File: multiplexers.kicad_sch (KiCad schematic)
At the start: 12 parts, among them U2 CD74HC4067M, U3 CD74HC4067M, U4 CD74HC4067M, U5 CD74HC4067M, U7 CD74HC4067M, U8 CD74HC4067M

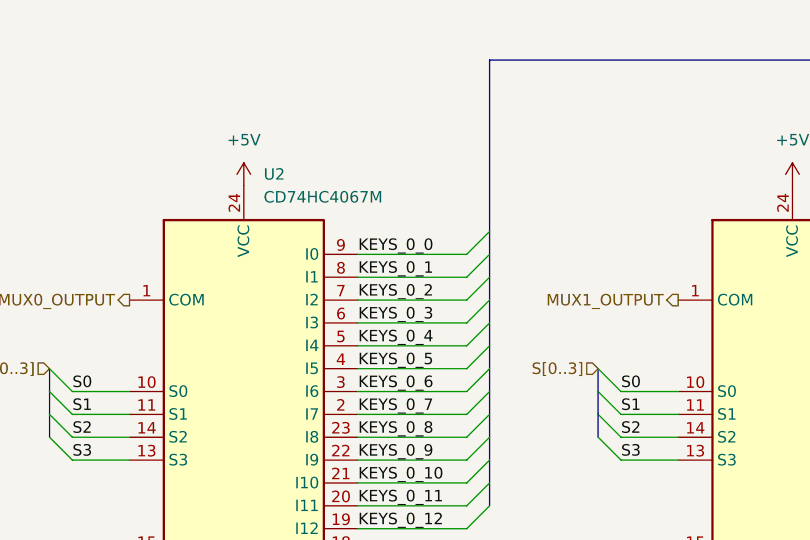
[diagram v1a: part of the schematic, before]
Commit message: make room for usb connectors
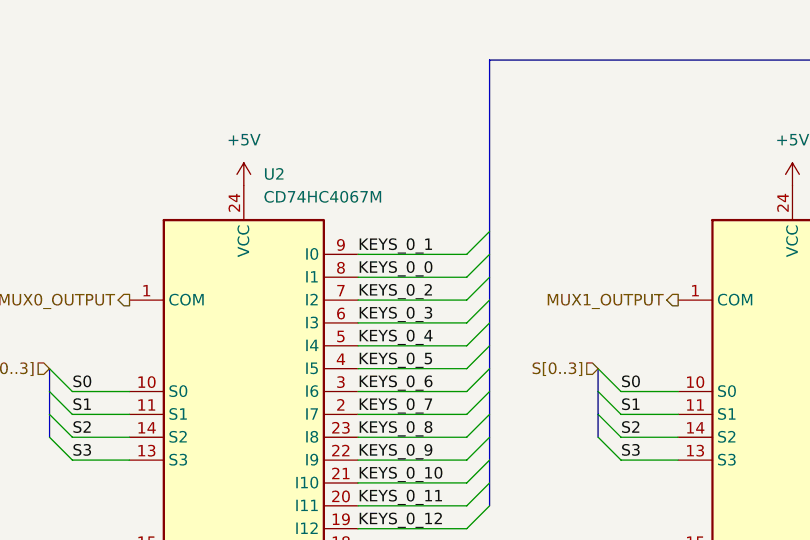
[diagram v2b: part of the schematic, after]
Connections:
- net KEYS_0_0: now also U2.8 (I1); no longer U2.9 (I0)
- net KEYS_0_1: now also U2.9 (I0); no longer U2.8 (I1)
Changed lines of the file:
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@@
     (effects (font (size 1.27 1.27)) (justify left bottom))
   )
-  (label "KEYS_0_0" (at 57.15 38.735 0) (fields_autoplaced)
+  (label "KEYS_0_0" (at 57.15 41.275 0) (fields_autoplaced)
     (effects (font (size 1.27 1.27)) (justify left bottom))
   )
@@
     (effects (font (size 1.27 1.27)) (justify left bottom))
   )
-  (label "KEYS_0_1" (at 57.15 41.275 0) (fields_autoplaced)
+  (label "KEYS_0_1" (at 57.15 38.735 0) (fields_autoplaced)
     (effects (font (size 1.27 1.27)) (justify left bottom))
   )

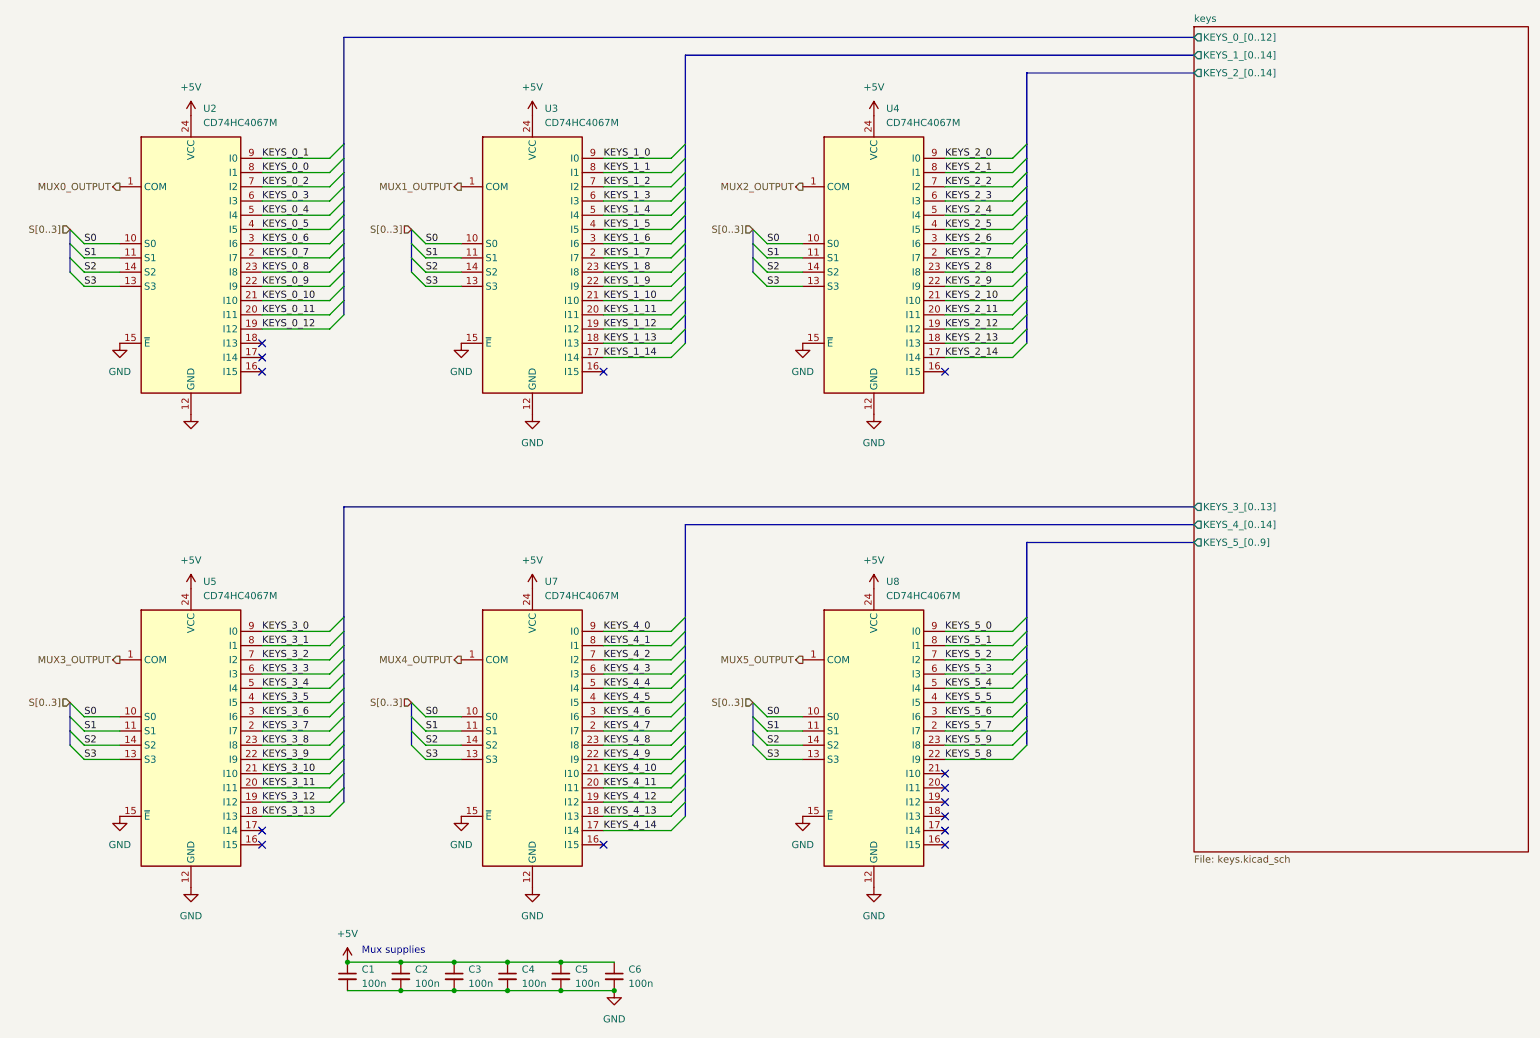
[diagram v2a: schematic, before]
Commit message: switch to SOIC multiplexers
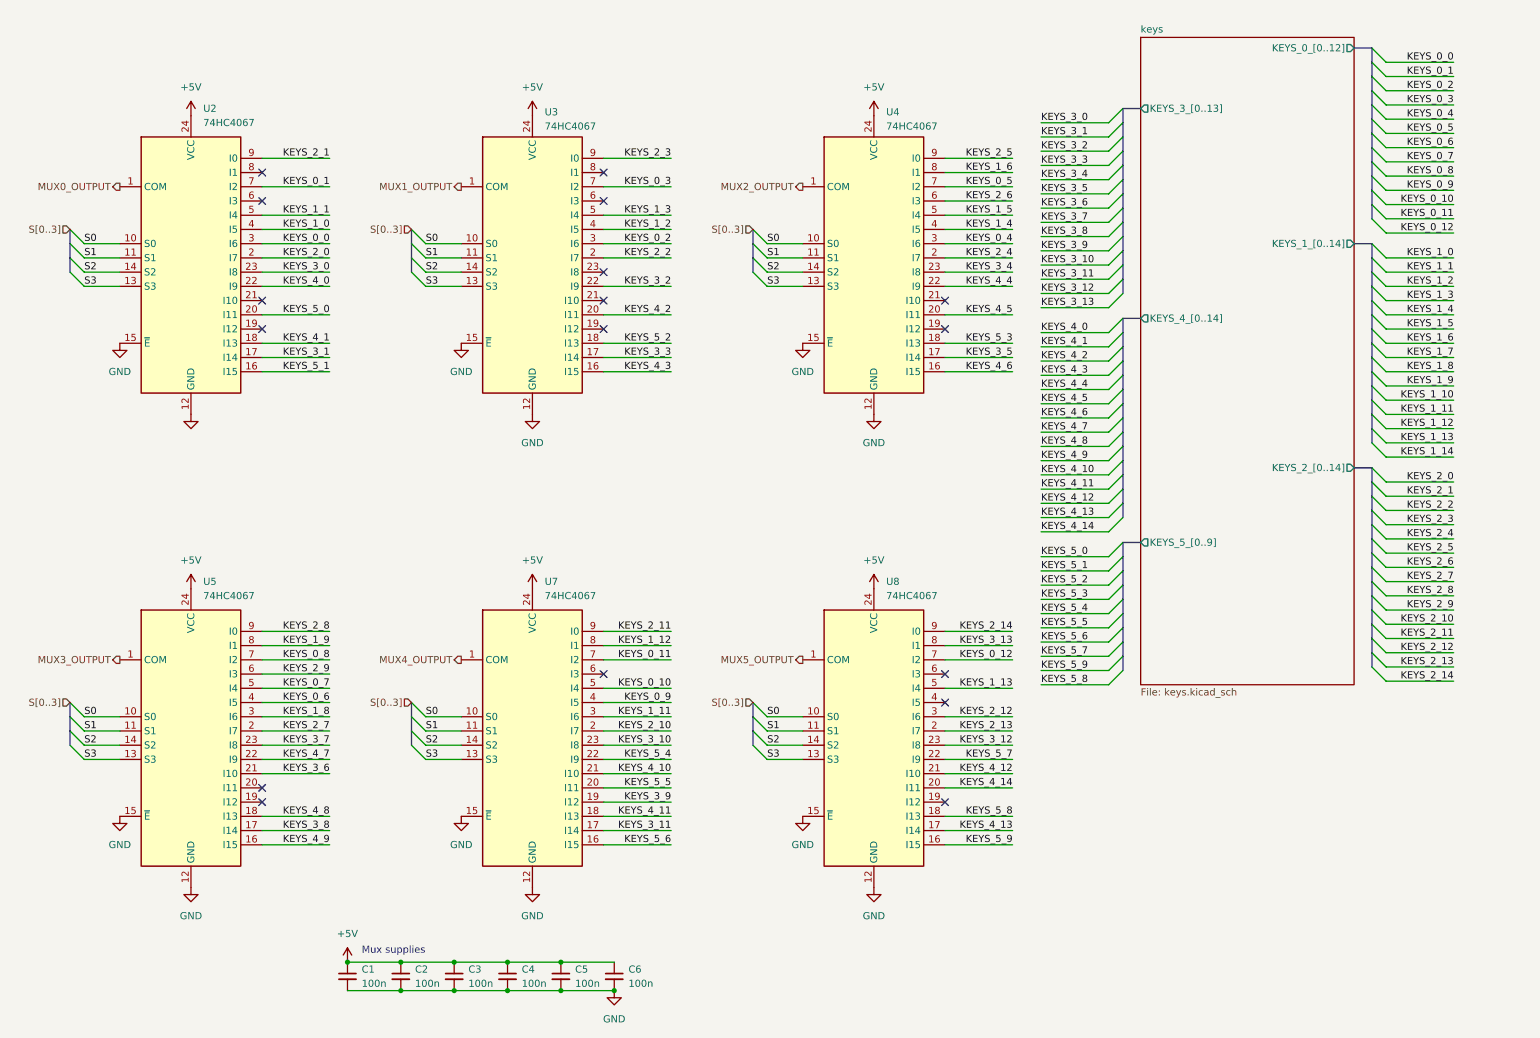
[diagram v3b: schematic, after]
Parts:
- U2, U3, U4, U5, U7, U8: value CD74HC4067M -> 74HC4067; footprint Package_SO:SOIC-24W_7.5x15.4mm_P1.27mm -> Package_SO:TSSOP-24_4.4x7.8mm_P0.65mm
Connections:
- net KEYS_0_0: now also U2.3 (I6); no longer U2.8 (I1)
- net KEYS_0_1: now also U2.7 (I2); no longer U2.9 (I0)
- net KEYS_0_10: now also U7.5 (I4); no longer U2.21 (I10)
- net KEYS_0_11: now also U7.7 (I2); no longer U2.20 (I11)
- net KEYS_0_12: now also U8.7 (I2); no longer U2.19 (I12)
- net KEYS_0_2: now also U3.3 (I6); no longer U2.7 (I2)
- net KEYS_0_3: now also U3.7 (I2); no longer U2.6 (I3)
- net KEYS_0_4: now also U4.3 (I6); no longer U2.5 (I4)
- net KEYS_0_5: now also U4.7 (I2); no longer U2.4 (I5)
- net KEYS_0_6: now also U5.4 (I5); no longer U2.3 (I6)
- net KEYS_0_7: now also U5.5 (I4); no longer U2.2 (I7)
- net KEYS_0_8: now also U5.7 (I2); no longer U2.23 (I8)
- net KEYS_0_9: now also U7.4 (I5); no longer U2.22 (I9)
- net KEYS_1_0: now also U2.4 (I5); no longer U3.9 (I0)
- net KEYS_1_1: now also U2.5 (I4); no longer U3.8 (I1)
- net KEYS_1_10: no longer U3.21 (I10)
- net KEYS_1_11: now also U7.3 (I6); no longer U3.20 (I11)
- net KEYS_1_12: now also U7.8 (I1); no longer U3.19 (I12)
- net KEYS_1_13: now also U8.5 (I4); no longer U3.18 (I13)
- net KEYS_1_14: no longer U3.17 (I14)
- net KEYS_1_2: now also U3.4 (I5); no longer U3.7 (I2)
- net KEYS_1_3: now also U3.5 (I4); no longer U3.6 (I3)
- net KEYS_1_4: now also U4.4 (I5); no longer U3.5 (I4)
- net KEYS_1_5: now also U4.5 (I4); no longer U3.4 (I5)
- net KEYS_1_6: now also U4.8 (I1); no longer U3.3 (I6)
- net KEYS_1_7: no longer U3.2 (I7)
- net KEYS_1_8: now also U5.3 (I6); no longer U3.23 (I8)
- net KEYS_1_9: now also U5.8 (I1); no longer U3.22 (I9)
- net KEYS_2_0: now also U2.2 (I7); no longer U4.9 (I0)
- net KEYS_2_1: now also U2.9 (I0); no longer U4.8 (I1)
- net KEYS_2_10: now also U7.2 (I7); no longer U4.21 (I10)
- net KEYS_2_11: now also U7.9 (I0); no longer U4.20 (I11)
- net KEYS_2_12: now also U8.3 (I6); no longer U4.19 (I12)
- net KEYS_2_13: now also U8.2 (I7); no longer U4.18 (I13)
- net KEYS_2_14: now also U8.9 (I0); no longer U4.17 (I14)
- net KEYS_2_2: now also U3.2 (I7); no longer U4.7 (I2)
- net KEYS_2_3: now also U3.9 (I0); no longer U4.6 (I3)
- net KEYS_2_4: now also U4.2 (I7); no longer U4.5 (I4)
- net KEYS_2_5: now also U4.9 (I0); no longer U4.4 (I5)
- net KEYS_2_6: now also U4.6 (I3); no longer U4.3 (I6)
- net KEYS_2_7: now also U5.2 (I7); no longer U4.2 (I7)
- net KEYS_2_8: now also U5.9 (I0); no longer U4.23 (I8)
- net KEYS_2_9: now also U5.6 (I3); no longer U4.22 (I9)
- net KEYS_3_0: now also U2.23 (I8); no longer U5.9 (I0)
- net KEYS_3_1: now also U2.17 (I14); no longer U5.8 (I1)
- net KEYS_3_10: now also U7.23 (I8); no longer U5.21 (I10)
- net KEYS_3_11: now also U7.17 (I14); no longer U5.20 (I11)
- net KEYS_3_12: now also U8.23 (I8); no longer U5.19 (I12)
- net KEYS_3_13: now also U8.8 (I1); no longer U5.18 (I13)
- net KEYS_3_2: now also U3.22 (I9); no longer U5.7 (I2)
- net KEYS_3_3: now also U3.17 (I14); no longer U5.6 (I3)
- net KEYS_3_4: now also U4.23 (I8); no longer U5.5 (I4)
- net KEYS_3_5: now also U4.17 (I14); no longer U5.4 (I5)
- net KEYS_3_6: now also U5.21 (I10); no longer U5.3 (I6)
- net KEYS_3_7: now also U5.23 (I8); no longer U5.2 (I7)
- net KEYS_3_8: now also U5.17 (I14); no longer U5.23 (I8)
- net KEYS_3_9: now also U7.19 (I12); no longer U5.22 (I9)
- net KEYS_4_0: now also U2.22 (I9); no longer U7.9 (I0)
- net KEYS_4_1: now also U2.18 (I13); no longer U7.8 (I1)
- net KEYS_4_11: now also U7.18 (I13); no longer U7.20 (I11)
- net KEYS_4_12: now also U8.21 (I10); no longer U7.19 (I12)
- net KEYS_4_13: now also U8.17 (I14); no longer U7.18 (I13)
- net KEYS_4_14: now also U8.20 (I11); no longer U7.17 (I14)
- net KEYS_4_2: now also U3.20 (I11); no longer U7.7 (I2)
- net KEYS_4_3: now also U3.16 (I15); no longer U7.6 (I3)
- net KEYS_4_4: now also U4.22 (I9); no longer U7.5 (I4)
- net KEYS_4_5: now also U4.20 (I11); no longer U7.4 (I5)
- net KEYS_4_6: now also U4.16 (I15); no longer U7.3 (I6)
- net KEYS_4_7: now also U5.22 (I9); no longer U7.2 (I7)
- net KEYS_4_8: now also U5.18 (I13); no longer U7.23 (I8)
- net KEYS_4_9: now also U5.16 (I15); no longer U7.22 (I9)
- net KEYS_5_0: now also U2.20 (I11); no longer U8.9 (I0)
- net KEYS_5_1: now also U2.16 (I15); no longer U8.8 (I1)
- net KEYS_5_2: now also U3.18 (I13); no longer U8.7 (I2)
- net KEYS_5_3: now also U4.18 (I13); no longer U8.6 (I3)
- net KEYS_5_4: now also U7.22 (I9); no longer U8.5 (I4)
- net KEYS_5_5: now also U7.20 (I11); no longer U8.4 (I5)
- net KEYS_5_6: now also U7.16 (I15); no longer U8.3 (I6)
- net KEYS_5_7: now also U8.22 (I9); no longer U8.2 (I7)
- net KEYS_5_8: now also U8.18 (I13); no longer U8.22 (I9)
- net KEYS_5_9: now also U8.16 (I15); no longer U8.23 (I8)
- no-connect marks 14 -> 17

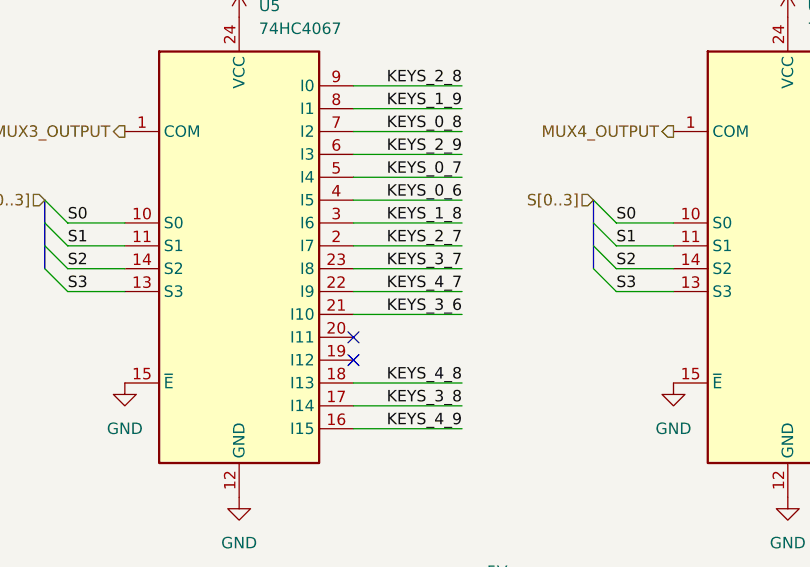
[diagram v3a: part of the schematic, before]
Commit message: fillet corners
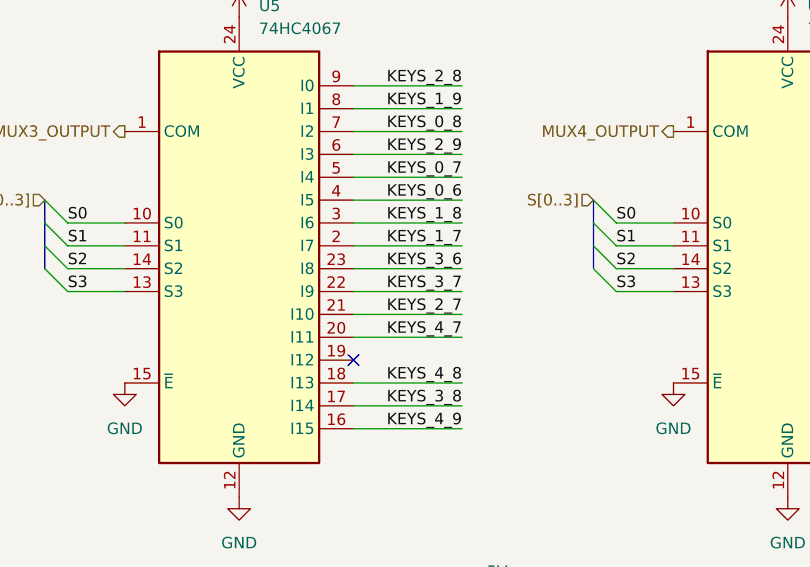
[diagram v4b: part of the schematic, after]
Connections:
- net KEYS_1_7: now also U5.2 (I7)
- net KEYS_2_7: now also U5.21 (I10); no longer U5.2 (I7)
- net KEYS_3_6: now also U5.23 (I8); no longer U5.21 (I10)
- net KEYS_3_7: now also U5.22 (I9); no longer U5.23 (I8)
- net KEYS_4_7: now also U5.20 (I11); no longer U5.22 (I9)
- no-connect marks 17 -> 16

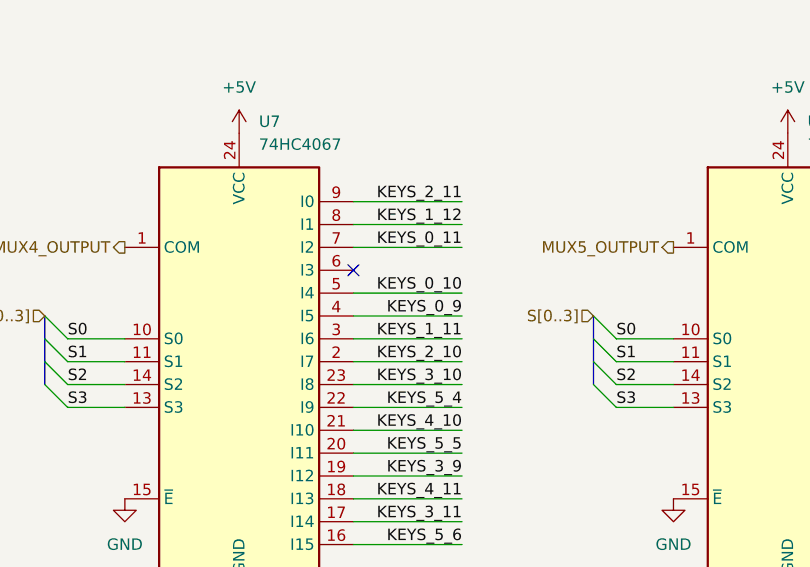
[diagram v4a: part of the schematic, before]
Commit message: fix LED footprint, add boot/reset jumpers
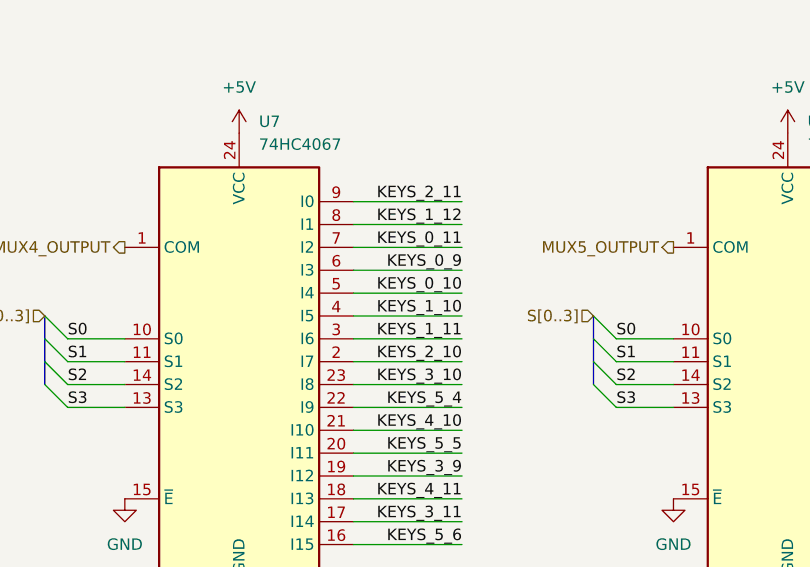
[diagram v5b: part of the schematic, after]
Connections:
- net KEYS_0_9: now also U7.6 (I3); no longer U7.4 (I5)
- net KEYS_1_10: now also U7.4 (I5)
- no-connect marks 16 -> 15
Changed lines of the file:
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@@
   (no_connect (at 179.07 64.135))
   (no_connect (at 57.15 153.67))
-  (no_connect (at 118.11 130.81))
   (no_connect (at 179.07 69.215))
   (no_connect (at 179.07 153.67))
@@
     (stroke (width 0) (type default))
   )
+  (wire (pts (xy 118.11 135.89) (xy 130.175 135.89))
+    (stroke (width 0) (type default))
+  )
   (bus (pts (xy 210.82 32.385) (xy 210.82 34.925))
     (stroke (width 0) (type default))
@@
     (stroke (width 0) (type default))
   )
-  (wire (pts (xy 118.11 135.89) (xy 130.175 135.89))
+  (wire (pts (xy 118.11 130.81) (xy 130.175 130.81))
     (stroke (width 0) (type default))
   )
@@
     (effects (font (size 1.27 1.27)) (justify right bottom))
   )
-  (label "KEYS_0_9" (at 130.175 135.89 180) (fields_autoplaced)
+  (label "KEYS_0_9" (at 130.175 130.81 180) (fields_autoplaced)
     (effects (font (size 1.27 1.27)) (justify right bottom))
   )
@@
     (effects (font (size 1.27 1.27)) (justify right bottom))
   )
+  (label "KEYS_1_10" (at 130.175 135.89 180) (fields_autoplaced)
+    (effects (font (size 1.27 1.27)) (justify right bottom))
+  )

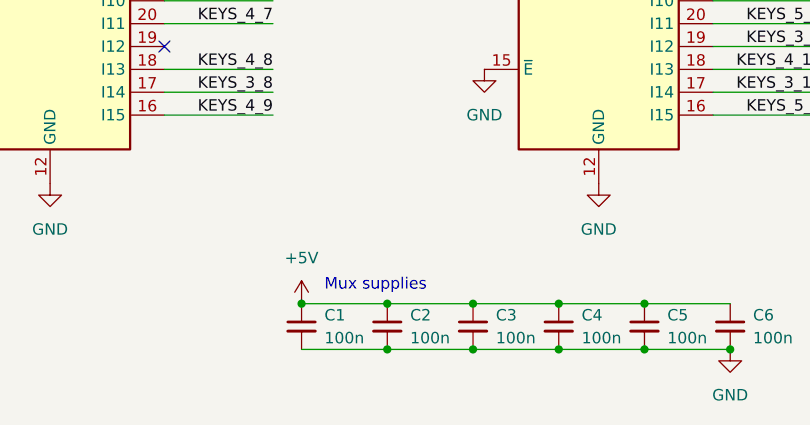
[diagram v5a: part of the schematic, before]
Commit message: add reverse polarity protection to LDO
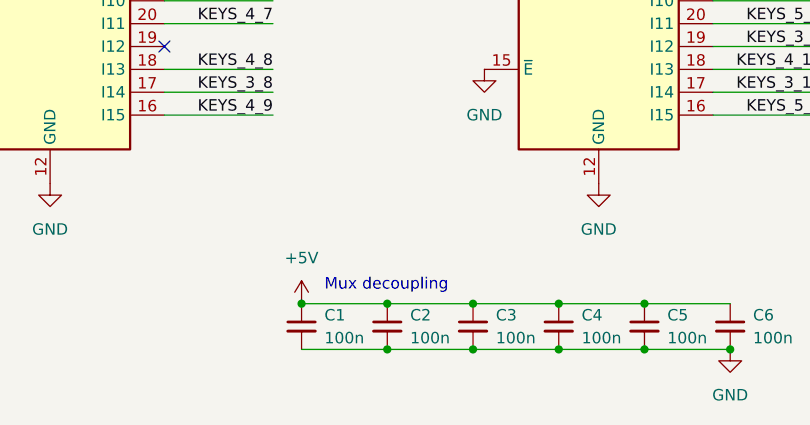
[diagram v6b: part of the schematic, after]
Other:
- note added: "Mux decoupling"
- note removed: "Mux supplies"
- title: (none) -> MoonBoard
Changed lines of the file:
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@@
 (kicad_sch (version 20230121) (generator eeschema)
   (paper "A4")
+  (title_block
+    (title "MoonBoard")
+  )
   (junction (at 110.49 187.325) (diameter 0) (color 0 0 0 0)
   )
@@
     (stroke (width 0) (type default))
   )
-  (text "Mux supplies" (at 74.93 180.975 0)
+  (text "Mux decoupling" (at 74.93 180.975 0)
     (effects (font (size 1.27 1.27)) (justify left bottom))
   )
